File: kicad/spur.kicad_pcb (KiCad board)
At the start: 2 copper layers, 35 parts, among them J1 USB_A, SW1 JS102000SAQN, U1 MIC5377YC5, U2 AT25SF081-MAHB-X, U3 STM32F401CBUx, Y1 24MHz

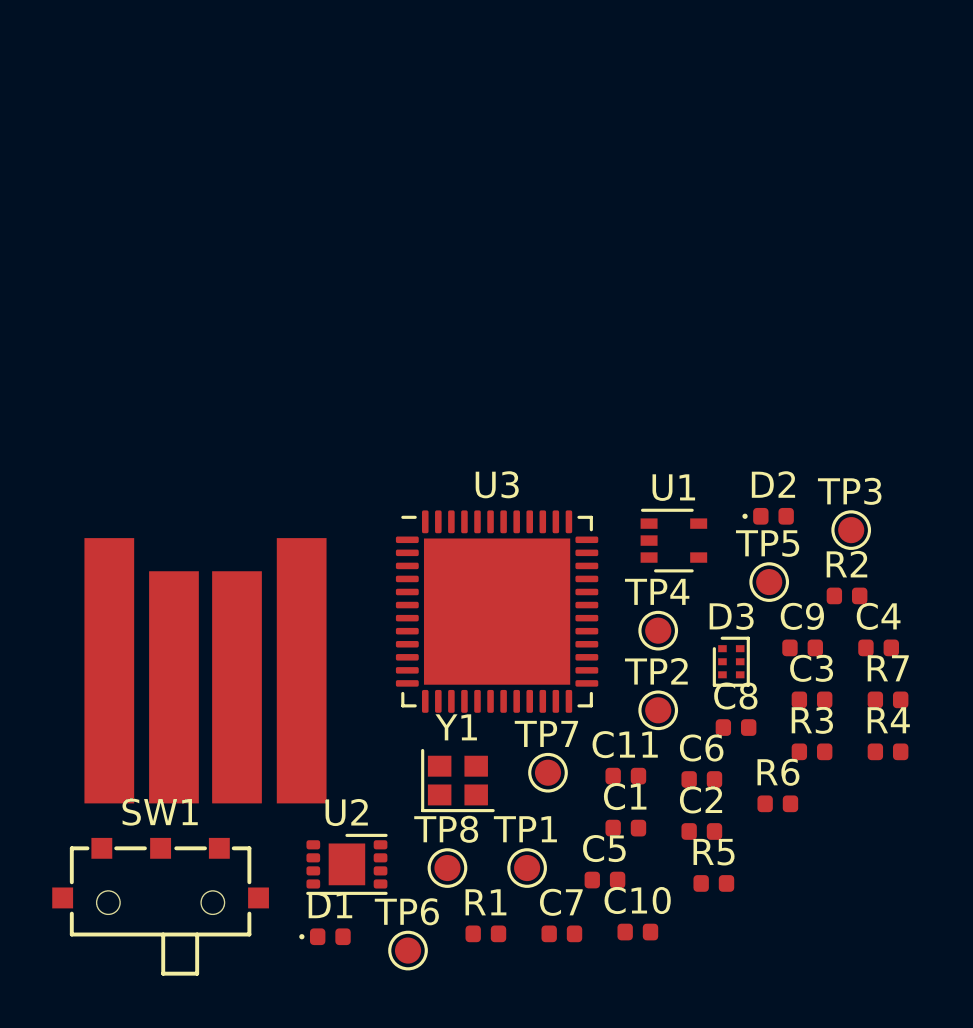
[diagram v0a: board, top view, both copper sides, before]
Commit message: Add PCB layout
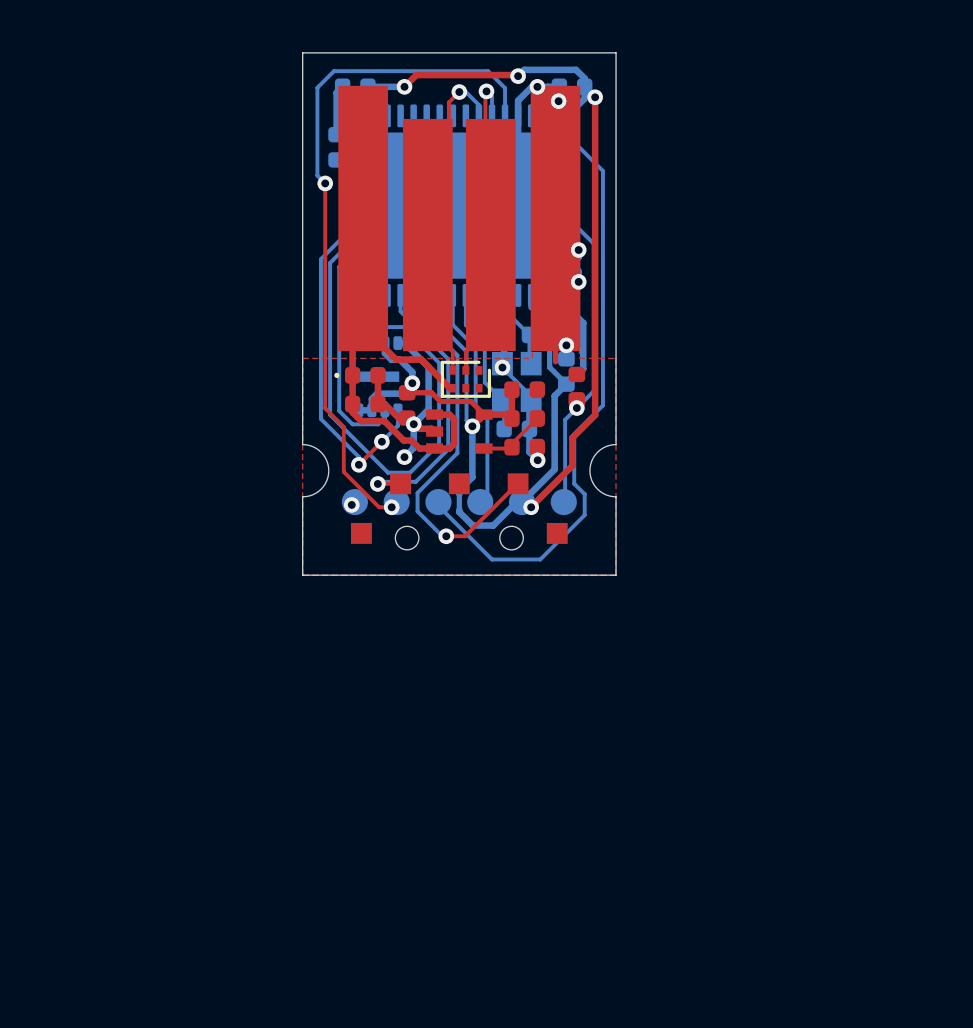
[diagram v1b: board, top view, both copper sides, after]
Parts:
- removed C11: 0.1u, Capacitor_SMD:C_0402_1005Metric
- removed D3: PRTR5V0U2X, Package_TO_SOT_SMD:SOT-886
- removed the R2 at (154.8, 94.8)
- removed R4, R5, R6: 10K, Resistor_SMD:R_0402_1005Metric
- removed TP7: SWDIO, TestPoint:TestPoint_Pad_D1.0mm
- removed TP8: SWCLK, TestPoint:TestPoint_Pad_D1.0mm
- C10, C4, C5, C6, C8, C9, TP1, TP2, TP3, TP4, U3, Y1: moved to B.Cu
- C7: value 4.7u -> 0.1u; moved to B.Cu
- D2: value GREEN -> PRTR5V0U2X; footprint LED_SMD:LED_0402_1005Metric -> Package_TO_SOT_SMD:SOT-886
- R1: value 10K -> 22K
- TP5: value TXO -> SWDIO; moved to B.Cu
- TP6: value RXI -> SWCLK; moved to B.Cu
- U2: footprint Package_SON:SON-8-1EP_3x2mm_P0.5mm_EP1.4x1.6mm -> spur:SON-8-1EP_3x2mm_P0.5mm_EP0.2x1.6mm; moved to B.Cu
- moved C8 28.5 mm to (136.0, 75.3), turned to 180 degrees
- moved C6 28.0 mm to (135.3, 77.6), turned to 90 degrees
- moved C10 23.6 mm to (144.1, 84.2), turned to 270 degrees
- moved C9 23.2 mm to (144.3, 75.3), turned to 180 degrees
- moved D1 21.5 mm to (136.4, 86.3)
- moved C7 21.5 mm to (144.1, 86.2), turned to 90 degrees
- moved J1 19.9 mm to (140.0, 79.7)
- moved R1 19.8 mm to (142.5, 88.0)
- moved C3 19.2 mm to (138.0, 87.5), turned to 270 degrees
- moved C1 19.1 mm to (136.4, 87.5)
- moved U2 18.7 mm to (136.9, 86.4), turned to 270 degrees
- moved C4 18.3 mm to (142.2, 84.8), turned to 180 degrees
- moved C2 18.2 mm to (142.5, 86.9)
- moved SW1 18.0 mm to (140.0, 92.4)
- moved C5 17.6 mm to (142.2, 88.4)
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- renumbered R3 to R2, R7 to R3
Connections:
- D2 pad 2: Net-(D2-Pad2) -> /D+
- R1 pad 2: /SPI_~CS -> Net-(R1-Pad2)
- R2 pad 1: Net-(R2-Pad2) -> Net-(R1-Pad2)
- SW1 pad 1: /BOOT_POS_1 -> /SW_POS1
- SW1 pad 2: +3V3 -> GND
- SW1 pad 3: /BOOT_POS_2 -> /SW_POS2
- TP5 pad 1: /UART_TXO -> /SWDIO
- TP6 pad 1: /UART_RXI -> /SWCLK
- U1 pad 4: Net-(R2-Pad2) -> Net-(R1-Pad2)
- U3 pad 10: Net-(U3-Pad10) -> /SW_POS1
- U3 pad 11: Net-(U3-Pad11) -> /SW_POS2
- U3 pad 12: /UART_TXO -> (no net)
- U3 pad 13: /UART_RXI -> (no net)
- U3 pad 18: Net-(U3-Pad18) -> (no net)
- U3 pad 19: Net-(U3-Pad19) -> (no net)
- U3 pad 2: Net-(U3-Pad2) -> (no net)
- U3 pad 20: Net-(U3-Pad20) -> (no net)
- U3 pad 21: Net-(U3-Pad21) -> (no net)
- U3 pad 25: Net-(U3-Pad25) -> (no net)
- U3 pad 26: Net-(U3-Pad26) -> (no net)
- U3 pad 27: Net-(U3-Pad27) -> (no net)
- U3 pad 28: Net-(U3-Pad28) -> (no net)
- U3 pad 29: Net-(U3-Pad29) -> (no net)
- U3 pad 3: Net-(U3-Pad3) -> (no net)
- U3 pad 30: Net-(U3-Pad30) -> (no net)
- U3 pad 31: Net-(U3-Pad31) -> (no net)
- U3 pad 38: Net-(U3-Pad38) -> (no net)
- U3 pad 39: Net-(U3-Pad39) -> (no net)
- U3 pad 4: Net-(U3-Pad4) -> (no net)
- U3 pad 40: Net-(U3-Pad40) -> (no net)
- U3 pad 41: Net-(U3-Pad41) -> (no net)
- U3 pad 42: Net-(U3-Pad42) -> (no net)
- U3 pad 43: Net-(U3-Pad43) -> (no net)
- U3 pad 45: Net-(U3-Pad45) -> (no net)
- U3 pad 46: Net-(U3-Pad46) -> (no net)
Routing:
- net +3V3: track 0.00 -> 69.0 mm, vias 0 -> 6
- net GND: track 0.00 -> 36.5 mm, vias 0 -> 10
- net VBUS: track 0.00 -> 28.1 mm
- net /SWDIO: track 0.00 -> 26.3 mm, vias 0 -> 2
- net /SWCLK: track 0.00 -> 23.8 mm
- net /SPI_MISO: track 0.00 -> 20.0 mm
- net /SW_POS1: track 0.00 -> 14.7 mm, vias 0 -> 1
- net /SPI_MOSI: track 0.00 -> 13.7 mm, vias 0 -> 2
- net /D-: track 0.00 -> 12.9 mm, vias 0 -> 1
- net /BOOT: track 0.00 -> 12.7 mm, vias 0 -> 1
- net /D+: track 0.00 -> 12.2 mm, vias 0 -> 1
- net /SW_POS2: track 0.00 -> 10.8 mm, vias 0 -> 1
- net /SPI_SCK: track 0.00 -> 9.28 mm
- net /~NRST: track 0.00 -> 8.58 mm
- net /OSC_OUT: track 0.00 -> 5.79 mm
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- added copper zone on F.Cu, net GND
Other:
- board outline added: 12 x 20 mm
- net class Default: trace_width 0.25 -> 0.15; via_dia 0.8 -> 0.6; via_drill 0.4 -> 0.3
- rule trace_min: 0.2 -> 0.15
- rule via_min_size: 0.4 -> 0.6
- board text added: "I.GLEN 2020"
- board text added: "SPUR v1.0"
- board text added: "UEFI BOOT SW"
